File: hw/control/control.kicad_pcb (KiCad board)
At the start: 2 copper layers, 200 x 100 mm, 130 parts, among them J101 Screw_Terminal_01x02, J102 Screw_Terminal_01x03, J103 Screw_Terminal_01x03, J301 Conn_02x05_Odd_Even, J302 Conn_01x04, J303 Raspberry_Pi_0_2_3, J304 Micro_SD_Card, J305 Conn_01x06, Q1001 BC807, Q1002 BC817, Q401 BC817, Q501 BC817, Q601 BC817, Q701 BC817, Q801 BC807, Q802 BC817, Q901 AOSP21357, Q902 IRF9540N, U1001 LM2678T-ADJ, U1101 SN74AHCT125D, U201 LM2596T-ADJ, U801 LM2678T-ADJ

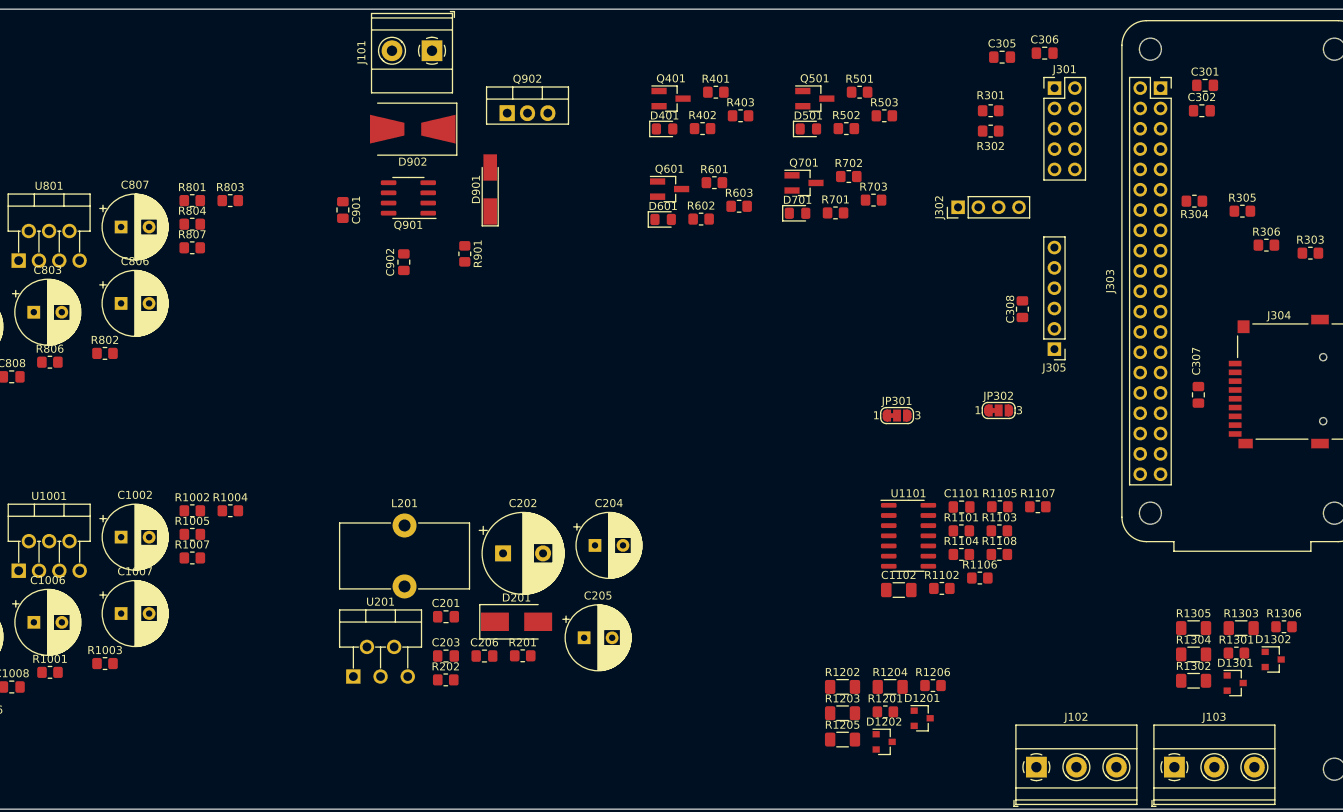
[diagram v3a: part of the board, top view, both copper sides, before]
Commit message: [hw] Assign control board footprints
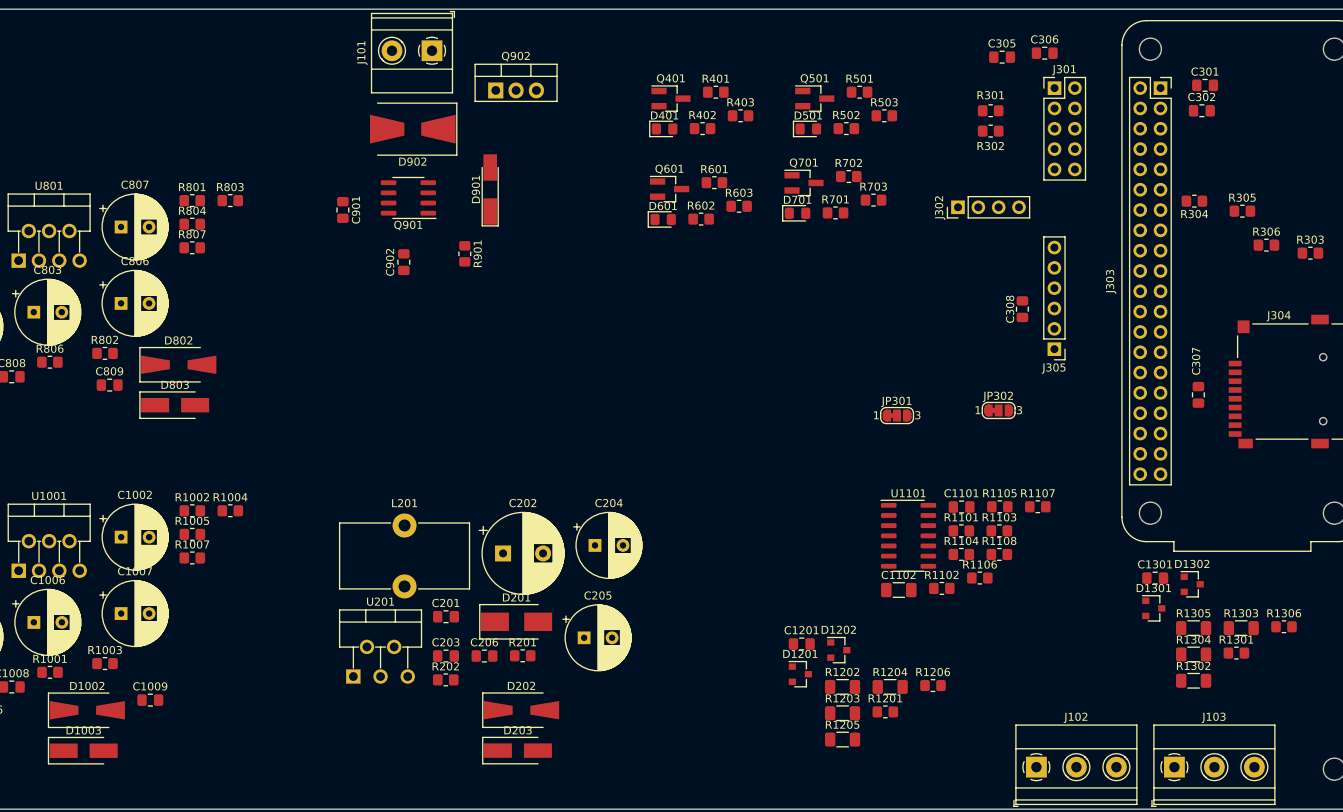
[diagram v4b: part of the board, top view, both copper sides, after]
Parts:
- added C1009: C, Capacitor_SMD:C_0805_2012Metric_Pad1.18x1.45mm_HandSolder, F.Cu at (90.5, 141.1)
- added C1201: 100n, Capacitor_SMD:C_0805_2012Metric_Pad1.18x1.45mm_HandSolder, F.Cu at (171.9, 134.1)
- added C1301: 100n, Capacitor_SMD:C_0805_2012Metric_Pad1.18x1.45mm_HandSolder, F.Cu at (216.1, 125.8)
- added C809: C, Capacitor_SMD:C_0805_2012Metric_Pad1.18x1.45mm_HandSolder, F.Cu at (85.4, 101.7)
- added D1002: SS14, Diode_SMD:D_SMA-SMB_Universal_Handsoldering, F.Cu at (82.6, 142.3)
- added D1003: TVS, Diode_SMD:D_SMA_Handsoldering, F.Cu at (82.2, 147.4)
- added D202: SS14, Diode_SMD:D_SMA-SMB_Universal_Handsoldering, F.Cu at (136.9, 142.3)
- added D203: TVS, Diode_SMD:D_SMA_Handsoldering, F.Cu at (136.4, 147.4)
- added D802: SS14, Diode_SMD:D_SMA-SMB_Universal_Handsoldering, F.Cu at (94.0, 99.2)
- added D803: TVS, Diode_SMD:D_SMA_Handsoldering, F.Cu at (93.6, 104.2)
- D1201, D1202, D1301, D1302: value BAV199TP -> BAT54S
- Q902: value IRF9540N -> IRF4905
- moved D1201 16.2 mm to (171.7, 137.8)
- moved D1301 13.8 mm to (215.9, 129.6)
- moved D1302 13.8 mm to (220.7, 126.6)
- moved D1202 12.8 mm to (176.6, 134.8)
- moved Q902 3.18 mm to (133.7, 64.9)
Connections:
- C201 pad 1: +5V -> Net-(C201-Pad1)
- C201 pad 2: Net-(C201-Pad2) -> +5V
- J303 pad 27: (no net) -> Net-(J303-Pad27)
- J303 pad 28: (no net) -> Net-(J303-Pad28)
- J303 pad 29: (no net) -> Net-(J303-Pad29)
- J303 pad 31: (no net) -> Net-(J303-Pad31)
- J303 pad 35: (no net) -> Net-(J303-Pad35)
- J303 pad 36: (no net) -> Net-(J303-Pad36)
- J303 pad 40: (no net) -> Net-(J303-Pad40)
- J304 pad 1: (no net) -> Net-(J304-Pad1)
- J304 pad 8: (no net) -> Net-(J304-Pad8)
- R201 pad 1: +5V -> Net-(C201-Pad1)
- R201 pad 2: Net-(C201-Pad2) -> +5V
- R202 pad 1: Net-(C201-Pad2) -> Net-(C201-Pad1)
- U1001 pad 5: (no net) -> Net-(U1001-Pad5)
- U201 pad 4: Net-(C201-Pad2) -> Net-(C201-Pad1)
- U801 pad 5: (no net) -> Net-(U801-Pad5)

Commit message: [hw] Calculate some values in control board
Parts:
- R1005, R805: value R -> 7K5

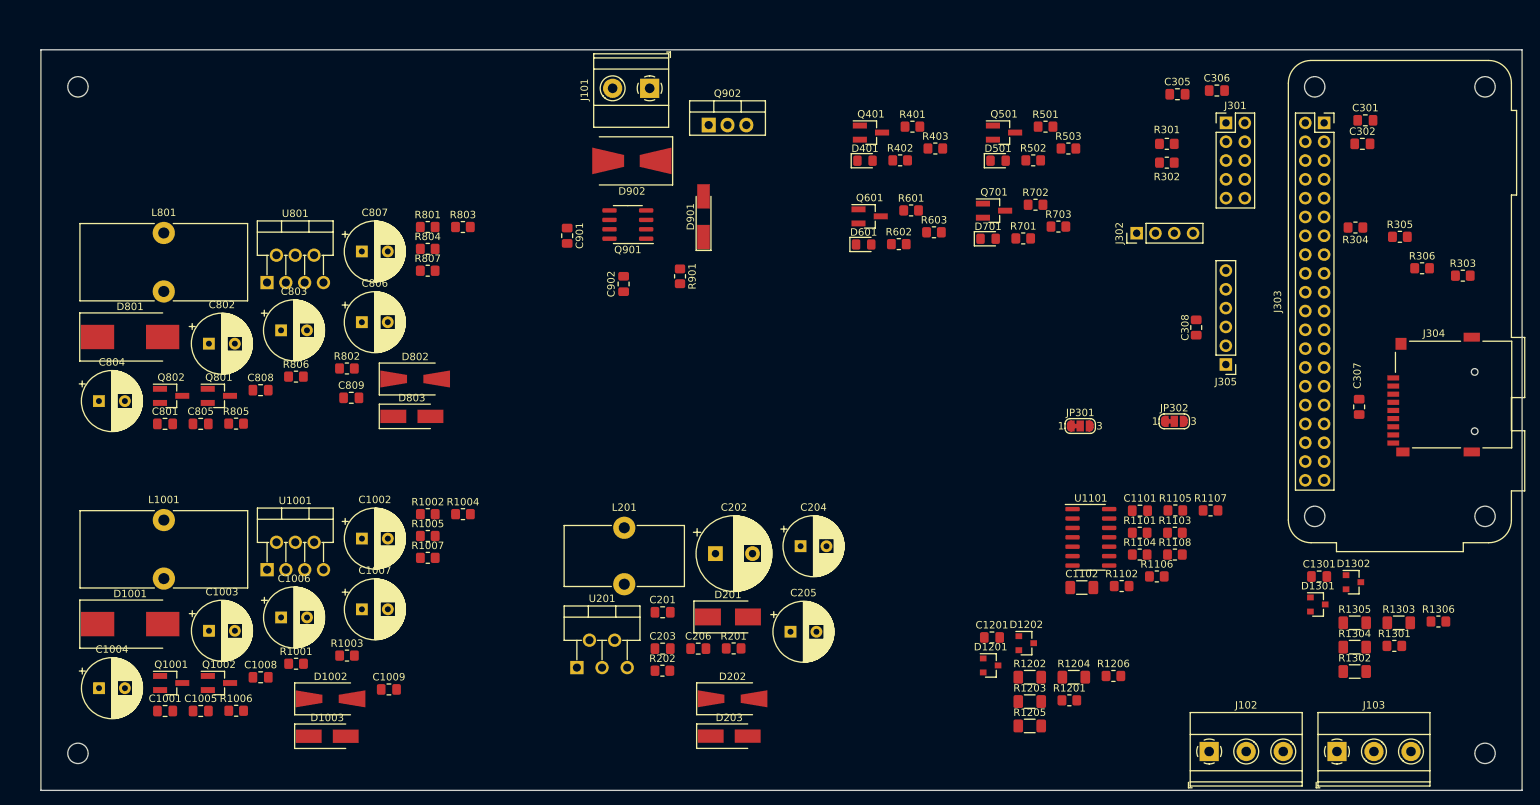
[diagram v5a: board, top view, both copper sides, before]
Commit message: [hw] Layout control input ptotection
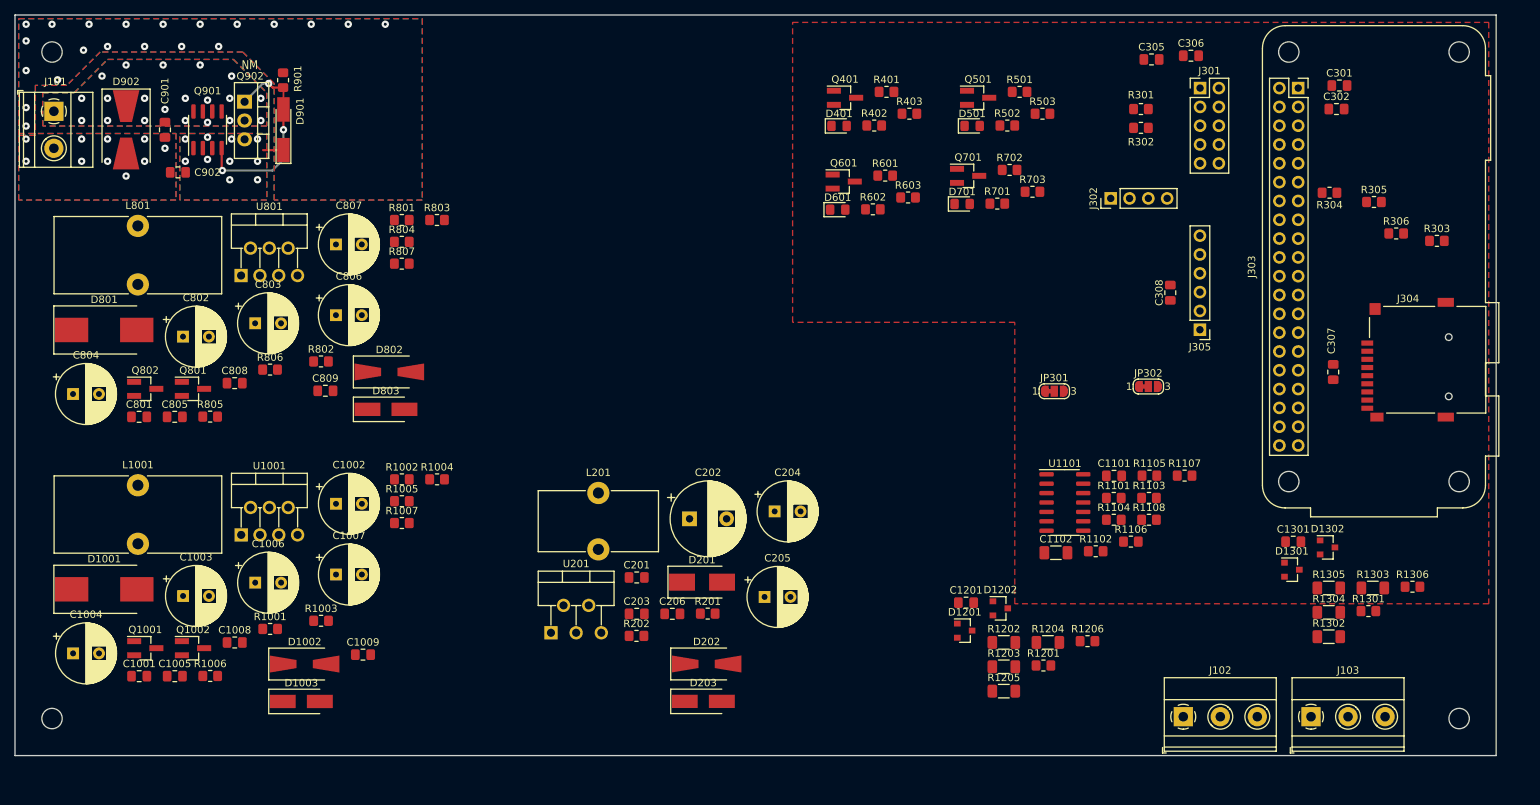
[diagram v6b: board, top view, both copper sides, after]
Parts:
- added g**: Not_Mounted, my:Not_Mounted, F.Cu at (70.2, 56.8)
- moved J101 80.5 mm to (45.2, 63.0), turned to 270 degrees
- moved D902 68.4 mm to (55.0, 65.5), turned to 270 degrees
- moved Q902 62.7 mm to (71.0, 61.7), turned to 270 degrees
- moved C902 62.0 mm to (62.0, 71.2), turned to 180 degrees
- moved R901 59.8 mm to (76.2, 58.8), turned to 90 degrees
- moved Q901 58.2 mm to (66.0, 65.5), turned to 90 degrees
- moved D901 57.9 mm to (76.2, 65.5)
- moved C901 56.2 mm to (60.2, 65.5)
- moved C1003 5.86 mm to (62.7, 128.4)
- moved C1004 5.86 mm to (47.8, 136.2)
- moved C1008 5.86 mm to (69.7, 134.7)
- moved C1201 5.86 mm to (168.4, 129.3)
- moved D1002 5.86 mm to (79.1, 137.6)
- moved D1201 5.86 mm to (168.2, 133.1)
- moved D202 5.86 mm to (133.4, 137.6)
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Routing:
- net Net-(D901-Pad2): track 0.00 -> 28.1 mm, vias 0 -> 3
- net /LED0 Power/VIN: track 0.00 -> 2.75 mm, vias 0 -> 10
- net GND: vias 0 -> 31
- net /Input Protection/V_A: vias 0 -> 20
- added copper zone on B.Cu, net /Input Protection/V_A
- added copper zone on F.Cu, net /Input Protection/V_A
- added copper zone on B.Cu, net /LED0 Power/VIN
- added copper zone on F.Cu, net /LED0 Power/VIN
- added copper zone on B.Cu, net GND
- added copper zone on F.Cu, net GND
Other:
- net class Default: via_dia 0.8 -> 1
- net class Driver Signal: via_dia 0.8 -> 1
- net class Power: via_dia 0.8 -> 1
- net class Raw Power: via_dia 0.8 -> 1
- net class Signal: via_dia 0.8 -> 1

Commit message: [hw] Layout LED power supply
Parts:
- moved R1004 186.1 mm to (-66.0, 202.5)
- moved R1005 179.2 mm to (-66.0, 199.8)
- moved R1007 175.4 mm to (-66.0, 194.2)
- moved R1003 164.7 mm to (-66.0, 205.5)
- moved Q1001 150.3 mm to (-69.8, 215.2)
- moved Q1002 148.0 mm to (-60.5, 215.5)
- moved R1006 144.4 mm to (-66.0, 197.0)
- moved C1007 128.7 mm to (-39.9, 162.6)
- moved D1001 128.7 mm to (-71.2, 164.6)
- moved C1001 128.7 mm to (-66.5, 176.3)
- moved C1002 128.7 mm to (-39.9, 153.0)
- moved C1003 128.7 mm to (-60.6, 165.4)
- moved C1004 128.7 mm to (-75.4, 173.2)
- moved C1005 128.7 mm to (-61.7, 176.3)
- moved C1006 128.7 mm to (-50.8, 163.7)
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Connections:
- J303 pad 27: Net-(J303-Pad27) -> (no net)
- J303 pad 28: Net-(J303-Pad28) -> (no net)
- J303 pad 29: Net-(J303-Pad29) -> (no net)
- J303 pad 31: Net-(J303-Pad31) -> (no net)
- J303 pad 35: Net-(J303-Pad35) -> (no net)
- J303 pad 36: Net-(J303-Pad36) -> (no net)
- J303 pad 40: Net-(J303-Pad40) -> (no net)
- J304 pad 1: Net-(J304-Pad1) -> (no net)
- J304 pad 8: Net-(J304-Pad8) -> (no net)
- U1001 pad 5: Net-(U1001-Pad5) -> (no net)
- U801 pad 5: Net-(U801-Pad5) -> (no net)
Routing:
- net /LED0 Power/ENABLE: track 0.00 -> 37.0 mm, vias 0 -> 1
- net Net-(C809-Pad2): track 0.00 -> 28.8 mm, vias 0 -> 1
- net Net-(Q802-Pad1): track 0.00 -> 9.06 mm
- net Net-(Q801-Pad1): track 0.00 -> 5.02 mm
- net GND: track 0.00 -> 3.35 mm, vias 31 -> 41
- net Net-(Q802-Pad3): track 0.00 -> 3.31 mm
- net +5V: track 0.00 -> 2.77 mm
- net Net-(C801-Pad2): track 0.00 -> 2.50 mm
- net /LED_PWR_EN0: track 0.00 -> 2.25 mm
- net Net-(C801-Pad1): vias 0 -> 4
- added copper zone on B.Cu, net /LED0 Power/VOUT
- added copper zone on F.Cu, net /LED0 Power/VOUT
- added copper zone on B.Cu, net Net-(C801-Pad1)
- added copper zone on F.Cu, net Net-(C801-Pad1)
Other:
- net class Default: trace_width 0.25 -> 0.3
- net class Raw Power: trace_width 0.25 -> 0.3
- net class Signal: trace_width 0.25 -> 0.3

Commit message: [hw] Replicate LED supply layout
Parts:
- moved C201 229.4 mm to (-84.8, 30.9)
- moved C202 229.4 mm to (-77.7, 23.0)
- moved C203 229.4 mm to (-84.8, 35.9)
- moved C204 229.4 mm to (-66.2, 22.0)
- moved C205 229.4 mm to (-67.5, 33.6)
- moved C206 229.4 mm to (-80.0, 35.9)
- moved D201 229.4 mm to (-76.0, 31.6)
- moved D202 229.4 mm to (-75.4, 42.6)
- moved D203 229.4 mm to (-75.8, 47.7)
- moved L201 229.4 mm to (-90.0, 19.5)
- moved R201 229.4 mm to (-75.2, 35.8)
- moved R202 229.4 mm to (-84.8, 38.8)
- moved U201 229.4 mm to (-96.4, 38.4)
- moved Q1001 204.9 mm to (105.0, 108.2), turned to 180 degrees
- moved R1003 200.4 mm to (109.2, 108.2), turned to 270 degrees
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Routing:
- net /LED1 Power/ENABLE: track 0.00 -> 37.0 mm, vias 0 -> 1
- net Net-(C1009-Pad2): track 0.00 -> 28.8 mm, vias 0 -> 1
- net /LED Driver/DATA_OUT0: track 0.00 -> 27.1 mm
- net /LED Driver/DATA_OUT1: track 0.00 -> 9.99 mm
- net Net-(Q1002-Pad1): track 0.00 -> 9.06 mm
- net Net-(Q1001-Pad1): track 0.00 -> 5.02 mm
- net GND: track 3.35 -> 6.70 mm, vias 41 -> 51
- net Net-(Q1002-Pad3): track 0.00 -> 3.31 mm
- net +5V: track 2.77 -> 5.54 mm
- net Net-(C1001-Pad2): track 0.00 -> 2.50 mm
- net /LED_PWR_EN1: track 0.00 -> 2.25 mm
- net Net-(C1001-Pad1): vias 0 -> 4
- added copper zone on B.Cu, net /LED1 Power/VOUT
- added copper zone on F.Cu, net /LED1 Power/VOUT
- added copper zone on B.Cu, net Net-(C1001-Pad1)
- added copper zone on F.Cu, net Net-(C1001-Pad1)
